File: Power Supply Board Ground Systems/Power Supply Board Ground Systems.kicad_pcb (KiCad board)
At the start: 2 copper layers, 203.2 x 50.8 mm, 38 parts, among them J1 POWER, J2 POWER OUT, SW1 SW_DIP_x01, SW2 SW_DIP_x01, SW3 SW_DIP_x01, SW4 SW_DIP_x01, SW5 SW_DIP_x01, SW6 SW_DIP_x01, SW7 SW_DIP_x01, SW8 SW_DIP_x01

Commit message: Some work
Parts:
- removed D10, D12, D14, D16: D_Small, Diode_SMD:D_SMA
- removed D11, D13, D15, D9: LED, LED_SMD:LED_0805_2012Metric
- removed R5, R6, R7, R8: 2.9K, Resistor_SMD:R_0603_1608Metric
- removed SW5, SW6, SW7, SW8: SW_DIP_x01, Rocker:RockerSwitch
- J2: footprint TerminalBlock_Phoenix:TerminalBlock_Phoenix_MPT-0,5-8-2.54_1x08_P2.54mm_Horizontal -> TerminalBlock_Phoenix:TerminalBlock_Phoenix_MKDS-1,5-4_1x04_P5.00mm_Horizontal
- moved H3 88.9 mm to (135.9, 40.6)
- moved H4 88.9 mm to (135.9, 66.0)
- moved J1 47.9 mm to (79.1, 70.6)
- moved J2 47.3 mm to (89.5, 32.2)
- moved D8 19.7 mm to (107.6, 30.9), turned to 0 degrees
- moved D7 17.4 mm to (105.9, 33.9), turned to 0 degrees
- moved R4 14.9 mm to (109.2, 33.9), turned to 0 degrees
- moved D5 10.4 mm to (95.4, 37.7), turned to 0 degrees
- moved R3 7.49 mm to (98.7, 37.7), turned to 0 degrees
- moved D6 6.96 mm to (97.2, 34.8), turned to 0 degrees
- moved D3 6.50 mm to (68.2, 38.1)
- moved R2 6.50 mm to (64.9, 38.0)
- moved D4 6.50 mm to (66.5, 35.2)
- moved R1 4.69 mm to (53.9, 34.0)
- moved D1 4.69 mm to (57.3, 34.0)
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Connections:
- J2 pad 1: OUT8 -> OUT4
- J2 pad 2: OUT7 -> OUT3
- J2 pad 3: OUT6 -> OUT2
- J2 pad 4: OUT5 -> OUT1
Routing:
- net POW IN: track 0.00 -> 100.8 mm
- net PSW4: track 0.00 -> 31.4 mm
- net PSW1: track 0.00 -> 30.9 mm
- net PSW3: track 0.00 -> 26.8 mm
- net PSW2: track 0.00 -> 26.3 mm
- net OUT1: track 0.00 -> 20.6 mm
- net OUT4: track 0.00 -> 20.0 mm
- net OUT2: track 0.00 -> 15.4 mm
- net OUT3: track 0.00 -> 15.0 mm
- net Net-(D3-Pad2): track 0.00 -> 1.61 mm
- net Net-(D1-Pad2): track 0.00 -> 1.61 mm
- net Net-(D7-Pad2): track 0.00 -> 1.59 mm
- net Net-(D5-Pad2): track 0.00 -> 1.58 mm
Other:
- board size 203.2 x 50.8 mm -> 114.3 x 50.8 mm
- board text added: "AARHUS WUZ HERE"
- board text added: "GND"
- board text added: "IN"
- board text added: "OUT"
- board text added: "POWER DIVIDER"
- board text added: "PWR"

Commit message: PT Board Moment
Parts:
- moved H1 1.27 mm to (30.5, 40.6)
- moved H2 1.27 mm to (30.5, 66.0)
- moved H3 1.27 mm to (134.6, 40.6)
- moved H4 1.27 mm to (134.6, 66.0)
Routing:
- net POW IN: track 100.8 -> 108.9 mm
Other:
- board text added: "CH1"
- board text added: "CH2"
- board text added: "CH3"
- board text added: "CH4"
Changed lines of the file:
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@@
     (property "Sheetname" "")
     (attr smd)
-    (fp_text reference "R4" (at 0 0 90) (layer "F.SilkS")
+    (fp_text reference "R4" (at -0.005 0.02 90) (layer "F.SilkS")
       (effects (font (size 0.5 0.5) (thickness 0.1)))
     )
@@
   )
   (footprint "MountingHole:MountingHole_3.2mm_M3_Pad_TopBottom" (layer "F.Cu")
-    (at 135.89 66.04)
+    (at 134.62 66.04)
     (descr "Mounting Hole 3.2mm, M3")
     (tags "mounting hole 3.2mm m3")
@@
     (property "Sheetname" "")
     (attr through_hole)
-    (fp_text reference "J2" (at 7.5 -6.26) (layer "F.SilkS")
+    (fp_text reference "J2" (at 7.5 -6.26) (layer "F.SilkS") hide
       (effects (font (size 1 1) (thickness 0.15)))
     )
@@
     (property "Sheetname" "")
     (attr through_hole)
-    (fp_text reference "J1" (at 2.45 -6.315) (layer "F.SilkS")
+    (fp_text reference "J1" (at 2.45 -6.315) (layer "F.SilkS") hide
       (effects (font (size 1 1) (thickness 0.15)))
     )
@@
   )
   (footprint "MountingHole:MountingHole_3.2mm_M3_Pad_TopBottom" (layer "F.Cu")
-    (at 29.21 66.04)
+    (at 30.48 66.04)
     (descr "Mounting Hole 3.2mm, M3")
     (tags "mounting hole 3.2mm m3")
@@
   )
   (footprint "MountingHole:MountingHole_3.2mm_M3_Pad_TopBottom" (layer "F.Cu")
-    (at 135.89 40.64)
+    (at 134.62 40.64)
     (descr "Mounting Hole 3.2mm, M3")
     (tags "mounting hole 3.2mm m3")
@@
   )
   (footprint "MountingHole:MountingHole_3.2mm_M3_Pad_TopBottom" (layer "F.Cu")
-    (at 29.21 40.64)
+    (at 30.48 40.64)
     (descr "Mounting Hole 3.2mm, M3")
     (tags "mounting hole 3.2mm m3")
@@
   )
   (gr_rect (start 25.4 25.4) (end 139.7 76.2) (layer "Edge.Cuts") (width 0.1) (fill none))
-  (gr_text "AARHUS WUZ HERE" (at 81.93 39.31) (layer "B.SilkS")
+  (gr_text "AARHUS WUZ HERE" (at 82.71 41.18) (layer "B.SilkS")
     (effects (font (size 1 1) (thickness 0.15)) (justify mirror))
   )
-  (gr_text "POWER DIVIDER" (at 100.01 69.12) (layer "F.SilkS")
-    (effects (font (size 1.5 1.5) (thickness 0.3)))
+  (gr_text "CH4" (at 89.635216 26.4 180) (layer "F.SilkS")
+    (effects (font (size 1 1) (thickness 0.15)))
+  )
+  (gr_text "POWER DIVIDER" (at 108.26 71.78) (layer "F.SilkS")
+    (effects (font (size 2 2) (thickness 0.3)))
+  )
+  (gr_text "POWER DIVIDER" (at 57.77 71.78) (layer "F.SilkS")
+    (effects (font (size 2 2) (thickness 0.3)))
   )
   (gr_text "PWR" (at 88.81 75.06) (layer "F.SilkS")
@@
     (effects (font (size 1 1) (thickness 0.15)))
   )
+  (gr_text "CH1" (at 74.357392 26.4 180) (layer "F.SilkS")
+    (effects (font (size 1 1) (thickness 0.15)))
+  )
   (gr_text "OUT" (at 128.53 28.92 180) (layer "F.SilkS")
     (effects (font (size 3 3) (thickness 0.3)))
@@
     (effects (font (size 3 3) (thickness 0.3)))
   )
+  (gr_text "CH2" (at 79.45 26.4 180) (layer "F.SilkS")
+    (effects (font (size 1 1) (thickness 0.15)))
+  )
   (gr_text "IN" (at 37.03 72.82) (layer "F.SilkS")
     (effects (font (size 3 3) (thickness 0.3)))
+  )
+  (gr_text "CH3" (at 84.542608 26.4 180) (layer "F.SilkS")
+    (effects (font (size 1 1) (thickness 0.15)))
   )
   (gr_text "OUT" (at 37.18 28.92 180) (layer "F.SilkS")
@@
   (segment (start 119.58 36.92) (end 113.54 30.88) (width 1) (layer "F.Cu") (net 12))
   (segment (start 110.06 32.85) (end 109.64 32.43) (width 0.3) (layer "F.Cu") (net 12))
-  (segment (start 80.58 65.71) (end 84.1 69.23) (width 3) (layer "F.Cu") (net 13))
-  (segment (start 119.58 59.73) (end 113.67 65.64) (width 3) (layer "F.Cu") (net 13))
-  (segment (start 47.03 65.71) (end 72.74 65.71) (width 3) (layer "F.Cu") (net 13))
-  (segment (start 89.085 65.64) (end 84.1 70.625) (width 3) (layer "F.Cu") (net 13))
-  (segment (start 45.15 59.73) (end 45.15 63.83) (width 3) (layer "F.Cu") (net 13))
-  (segment (start 84.1 69.23) (end 84.1 70.625) (width 3) (layer "F.Cu") (net 13))
-  (segment (start 69.96 59.73) (end 69.96 62.93) (width 3) (layer "F.Cu") (net 13))
-  (segment (start 94.77 59.73) (end 94.77 63.09) (width 3) (layer "F.Cu") (net 13))
-  (segment (start 69.96 62.93) (end 72.74 65.71) (width 3) (layer "F.Cu") (net 13))
-  (segment (start 72.74 65.71) (end 80.58 65.71) (width 3) (layer "F.Cu") (net 13))
-  (segment (start 94.77 63.09) (end 97.32 65.64) (width 3) (layer "F.Cu") (net 13))
-  (segment (start 113.67 65.64) (end 97.32 65.64) (width 3) (layer "F.Cu") (net 13))
-  (segment (start 97.32 65.64) (end 89.085 65.64) (width 3) (layer "F.Cu") (net 13))
-  (segment (start 45.15 63.83) (end 47.03 65.71) (width 3) (layer "F.Cu") (net 13))
+  (segment (start 119.58 62.98) (end 115.91 66.65) (width 1) (layer "F.Cu") (net 13))
+  (segment (start 84.1 70.625) (end 84.1 68.786523) (width 3) (layer "F.Cu") (net 13))
+  (segment (start 45.15 64.03) (end 47.71 66.59) (width 1) (layer "F.Cu") (net 13))
+  (segment (start 45.15 59.73) (end 45.15 64.03) (width 1) (layer "F.Cu") (net 13))
+  (segment (start 90.92 66.66) (end 90.31 66.66) (width 1) (layer "F.Cu") (net 13))
+  (segment (start 88.065 66.66) (end 90.31 66.66) (width 3) (layer "F.Cu") (net 13))
+  (segment (start 81.903477 66.59) (end 73.66 66.59) (width 3) (layer "F.Cu") (net 13))
+  (segment (start 119.58 59.73) (end 119.58 62.98) (width 1) (layer "F.Cu") (net 13))
+  (segment (start 94.77 59.73) (end 94.77 62.81) (width 1) (layer "F.Cu") (net 13))
+  (segment (start 73.66 66.59) (end 47.71 66.59) (width 3) (layer "F.Cu") (net 13))
+  (segment (start 90.31 66.66) (end 90.41 66.56) (width 3) (layer "F.Cu") (net 13))
+  (segment (start 88.065 66.66) (end 115.9 66.66) (width 3) (layer "F.Cu") (net 13))
+  (segment (start 94.77 62.81) (end 90.92 66.66) (width 1) (layer "F.Cu") (net 13))
+  (segment (start 84.1 68.786523) (end 81.903477 66.59) (width 3) (layer "F.Cu") (net 13))
+  (segment (start 115.9 66.66) (end 115.91 66.65) (width 3) (layer "F.Cu") (net 13))
+  (segment (start 69.96 59.73) (end 69.96 62.89) (width 1) (layer "F.Cu") (net 13))
+  (segment (start 69.96 62.89) (end 73.66 66.59) (width 1) (layer "F.Cu") (net 13))
+  (segment (start 84.1 70.625) (end 88.065 66.66) (width 3) (layer "F.Cu") (net 13))
   (zone (net 14) (net_name "GND") (layer "B.Cu") (hatch edge 0.508)
     (connect_pads yes (clearance 0.508))

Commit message: Idk lol some format changes
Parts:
- moved D8 36.9 mm to (121.3, 65.2), turned to -90 degrees
- moved D2 36.1 mm to (44.1, 65.3), turned to -90 degrees
- moved R4 34.1 mm to (118.3, 66.8), turned to -90 degrees
- moved R1 33.6 mm to (47.0, 66.9), turned to -90 degrees
- moved D7 32.0 mm to (118.3, 63.4), turned to -90 degrees
- moved D1 31.3 mm to (47.0, 63.5), turned to -90 degrees
- moved D6 30.3 mm to (96.1, 65.1), turned to -90 degrees
- moved D4 30.1 mm to (69.2, 65.1), turned to -90 degrees
- moved R2 29.6 mm to (72.1, 66.8), turned to -90 degrees
- moved R3 29.5 mm to (93.3, 66.7), turned to -90 degrees
- moved D5 25.7 mm to (93.2, 63.3), turned to -90 degrees
- moved D3 25.6 mm to (72.1, 63.4), turned to -90 degrees
- moved SW4 4.23 mm to (121.2, 48.8)
- moved SW3 4.14 mm to (96.2, 48.8)
- moved SW1 4.06 mm to (44.0, 48.8)
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- renumbered H3 to Hw
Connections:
- D1 pad 1: OUT1 -> PSW1
- D2 pad 1: OUT1 -> PSW1
- D2 pad 2: PSW1 -> POW IN
- D3 pad 1: OUT2 -> PSW2
- D4 pad 1: OUT2 -> PSW2
- D4 pad 2: PSW2 -> POW IN
- D5 pad 1: OUT3 -> PSW3
- D6 pad 1: OUT3 -> PSW3
- D6 pad 2: PSW3 -> POW IN
- D7 pad 1: OUT4 -> PSW4
- D8 pad 1: OUT4 -> PSW4
- D8 pad 2: PSW4 -> POW IN
- R1 pad 2: PSW1 -> POW IN
- R2 pad 2: PSW2 -> POW IN
- R3 pad 2: PSW3 -> POW IN
- R4 pad 2: PSW4 -> POW IN
- SW1 pad 1: POW IN -> PSW1
- SW1 pad 2: PSW1 -> OUT1
- SW2 pad 1: POW IN -> PSW2
- SW2 pad 2: PSW2 -> OUT2
- SW3 pad 1: POW IN -> PSW3
- SW3 pad 2: PSW3 -> OUT3
- SW4 pad 1: POW IN -> PSW4
- SW4 pad 2: PSW4 -> OUT4
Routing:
- net PSW4: track 31.4 -> 10.9 mm
- net PSW1: track 30.9 -> 10.8 mm
- net OUT4: track 20.0 -> 38.4 mm
- net OUT1: track 20.6 -> 38.1 mm
- net PSW3: track 26.8 -> 10.5 mm
- net PSW2: track 26.3 -> 10.5 mm
- net OUT3: track 15.0 -> 26.0 mm
- net POW IN: track 108.9 -> 119.5 mm
- net OUT2: track 15.4 -> 25.4 mm

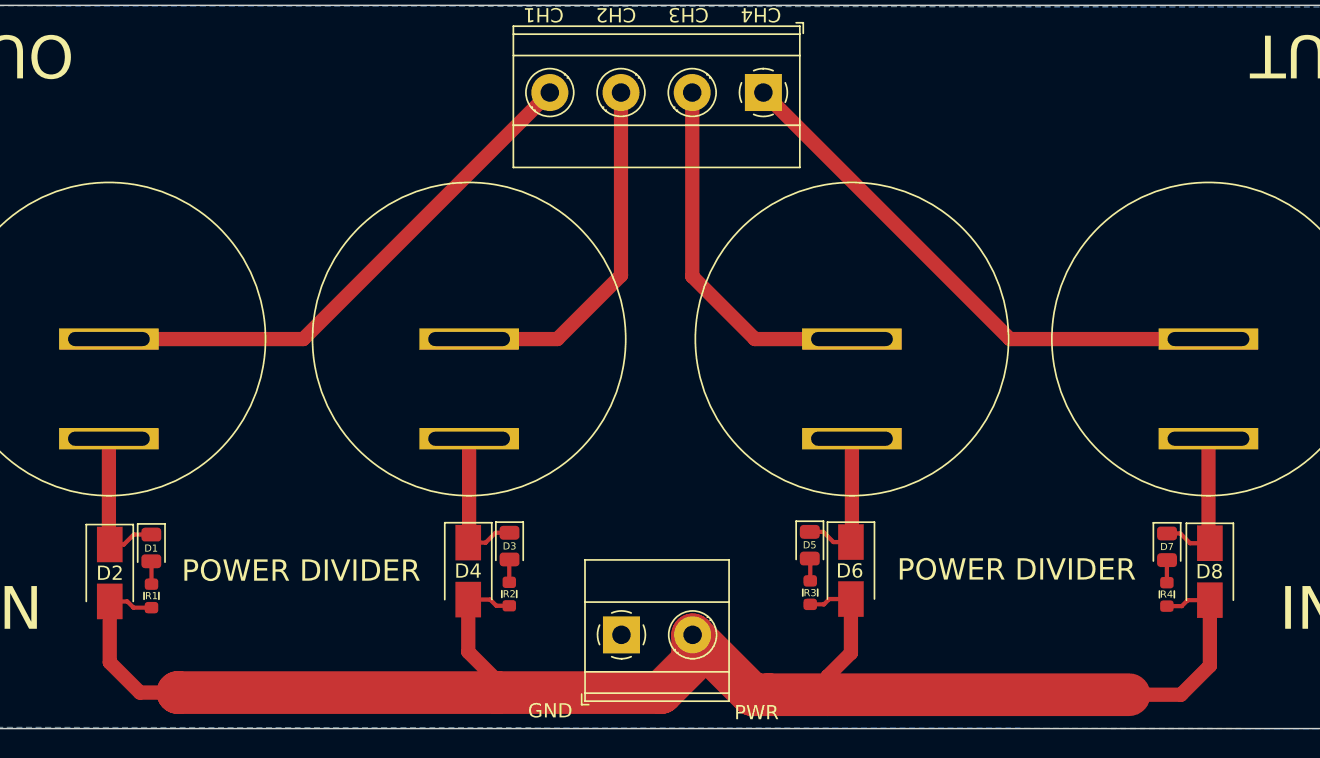
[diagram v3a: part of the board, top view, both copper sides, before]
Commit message: Reconfigured the LEDs
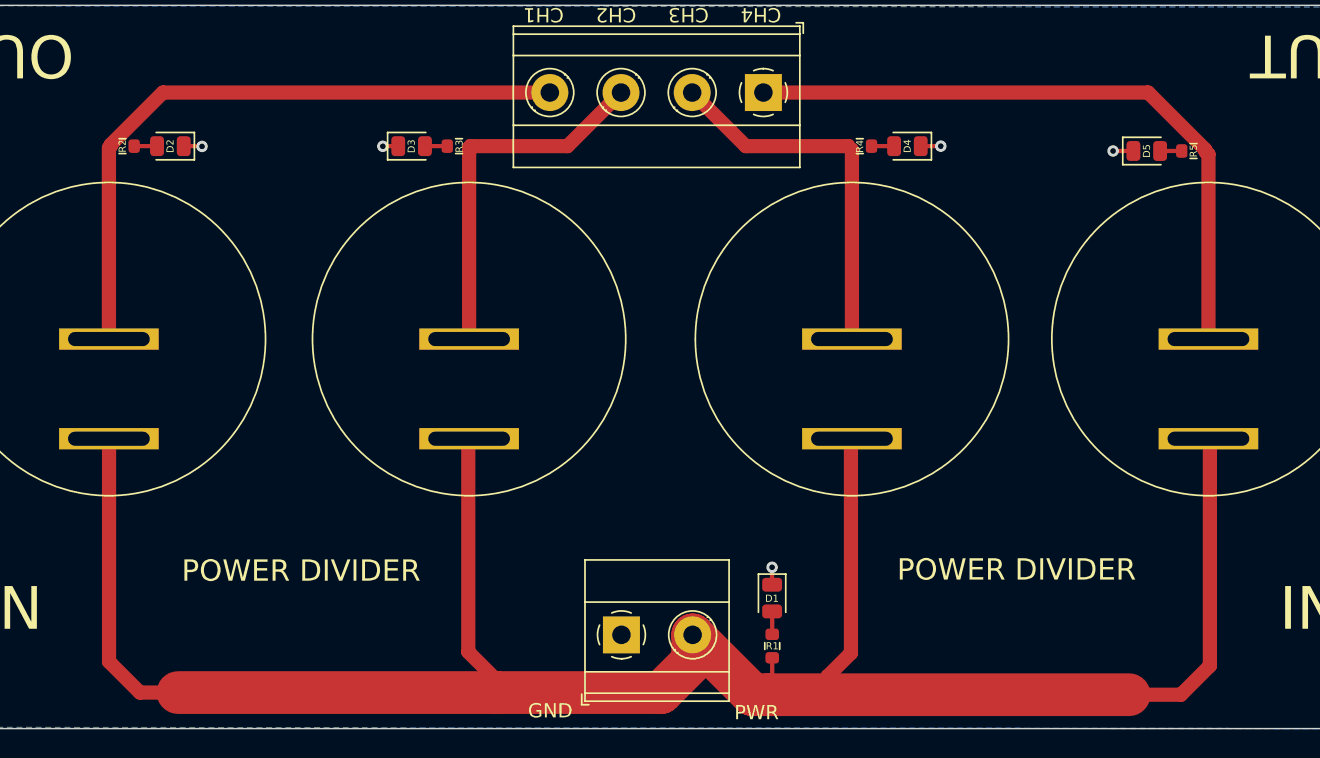
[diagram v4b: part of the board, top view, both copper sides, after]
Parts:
- removed the D2 at (44.1, 65.3)
- removed the D4 at (69.2, 65.1)
- removed D6, D8: D_Small, Diode_SMD:D_SMA
- added D5: LED, LED_SMD:LED_0805_2012Metric, F.Cu at (116.9, 35.6)
- added R5: 8K, Resistor_SMD:R_0603_1608Metric, F.Cu at (120.2, 35.6)
- R1, R2, R3, R4: value 2.9K -> 8K
- moved D1 43.7 mm to (90.6, 67.0)
- moved R1 43.7 mm to (90.6, 70.4)
- moved R2 41.6 mm to (45.0, 35.3), turned to 180 degrees
- moved R3 39.9 mm to (68.6, 35.3), turned to 0 degrees
- moved D3 39.6 mm to (65.3, 35.3), turned to 0 degrees
- moved R4 38.2 mm to (96.7, 35.3), turned to 180 degrees
- moved D2 36.8 mm to (48.3, 35.3), turned to 180 degrees
- moved D4 33.5 mm to (100.1, 35.3), turned to 180 degrees
- renumbered D3 to D2, D5 to D3, D7 to D4, Hw to H3
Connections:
- D1 pad 1: PSW1 -> GND
- D2 pad 1: PSW2 -> GND
- D3 pad 1: PSW3 -> GND
- D4 pad 1: PSW4 -> GND
- R2 pad 2: POW IN -> OUT1
- R3 pad 2: POW IN -> OUT2
- R4 pad 2: POW IN -> OUT3
- SW1 pad 1: PSW1 -> POW IN
- SW2 pad 1: PSW2 -> POW IN
- SW3 pad 1: PSW3 -> POW IN
- SW4 pad 1: PSW4 -> POW IN
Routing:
- net POW IN: track 119.5 -> 155.3 mm
- net PSW4: track 10.9 -> 0.00 mm
- net PSW1: track 10.8 -> 0.00 mm
- net PSW2: track 10.5 -> 0.00 mm
- net PSW3: track 10.5 -> 0.00 mm
- net OUT1: track 38.1 -> 46.1 mm
- net OUT4: track 38.4 -> 46.1 mm
- net GND: track 0.00 -> 6.44 mm, vias 0 -> 5
- net Net-(D5-Pad2): track 0.00 -> 1.53 mm

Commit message: Added stitches
Needs footprints made
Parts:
- removed SW1, SW2, SW3, SW4: SW_DIP_x01, Rocker:RockerSwitch
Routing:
- net POW IN: track 155.3 -> 0.00 mm
- net OUT4: track 46.1 -> 0.00 mm
- net OUT1: track 46.1 -> 0.00 mm
- net OUT3: track 26.2 -> 0.00 mm
- net OUT2: track 25.7 -> 0.00 mm
- net GND: track 6.44 -> 0.00 mm
- net Net-(D2-Pad2): track 1.61 -> 0.00 mm
- net Net-(D1-Pad2): track 1.61 -> 0.00 mm
- net Net-(D4-Pad2): track 1.58 -> 0.00 mm
- net Net-(D3-Pad2): track 1.57 -> 0.00 mm
- net Net-(D5-Pad2): track 1.53 -> 0.00 mm

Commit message: Re Done Power Supply Board
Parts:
- added D6: LED, LED_SMD:LED_0805_2012Metric, F.Cu at (66.5, 39.8)
- added D7: LED, LED_SMD:LED_0805_2012Metric, F.Cu at (74.2, 39.8)
- added D8: LED, LED_SMD:LED_0805_2012Metric, F.Cu at (81.9, 39.8)
- added D9: LED, LED_SMD:LED_0805_2012Metric, F.Cu at (89.6, 39.8)
- added R6: 8K, Resistor_SMD:R_0603_1608Metric, F.Cu at (69.0, 42.3)
- added R7: 8K, Resistor_SMD:R_0603_1608Metric, F.Cu at (76.7, 42.3)
- added R8: 8K, Resistor_SMD:R_0603_1608Metric, F.Cu at (84.4, 42.3)
- added R9: 8K, Resistor_SMD:R_0603_1608Metric, F.Cu at (92.1, 42.3)
- added SW1: SW_SPDT, E_Switch:100SP1T1B1M2QEH, F.Cu at (35.7, 46.5)
- added SW2: SW_SPDT, E_Switch:100SP1T1B1M2QEH, F.Cu at (43.4, 46.5)
- added SW3: SW_SPDT, E_Switch:100SP1T1B1M2QEH, F.Cu at (51.1, 46.5)
- added SW4: SW_SPDT, E_Switch:100SP1T1B1M2QEH, F.Cu at (58.8, 46.5)
- added SW5: SW_SPDT, E_Switch:100SP1T1B1M2QEH, F.Cu at (66.5, 46.5)
- added SW6: SW_SPDT, E_Switch:100SP1T1B1M2QEH, F.Cu at (74.2, 46.5)
- added SW7: SW_SPDT, E_Switch:100SP1T1B1M2QEH, F.Cu at (81.9, 46.5)
- added SW8: SW_SPDT, E_Switch:100SP1T1B1M2QEH, F.Cu at (89.5, 46.5)
- J2: footprint TerminalBlock_Phoenix:TerminalBlock_Phoenix_MKDS-1,5-4_1x04_P5.00mm_Horizontal -> TerminalBlock_Phoenix:TerminalBlock_Phoenix_MKDS-1,5-8_1x08_P5.00mm_Horizontal
- moved R5 59.3 mm to (61.3, 42.3)
- moved D5 58.2 mm to (58.8, 39.8), turned to -90 degrees
- moved D4 49.2 mm to (51.1, 39.8), turned to -90 degrees
- moved R4 43.7 mm to (53.6, 42.3), turned to 0 degrees
- moved H3 38.1 mm to (96.5, 38.1)
- moved H4 38.1 mm to (96.5, 63.5)
- moved R3 23.7 mm to (45.9, 42.3)
- moved D3 22.3 mm to (43.4, 39.8), turned to -90 degrees
- moved J1 20.0 mm to (60.0, 69.1)
- moved R1 19.0 mm to (71.6, 69.1), turned to 180 degrees
- moved D1 15.7 mm to (75.0, 69.1), turned to 180 degrees
- moved D2 13.4 mm to (35.7, 39.8), turned to -90 degrees
- moved J2 11.9 mm to (78.0, 31.8)
- moved R2 9.72 mm to (38.2, 42.3), turned to 0 degrees
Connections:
- J2 pad 1: OUT4 -> OUT8
- J2 pad 2: OUT3 -> OUT7
- J2 pad 3: OUT2 -> OUT6
- J2 pad 4: OUT1 -> OUT5
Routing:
- net POW IN: track 0.00 -> 123.4 mm
- net OUT8: track 0.00 -> 32.0 mm
- net OUT7: track 0.00 -> 30.4 mm
- net OUT6: track 0.00 -> 27.0 mm
- net OUT5: track 0.00 -> 24.2 mm
- net OUT4: track 0.00 -> 23.8 mm
- net OUT1: track 0.00 -> 23.3 mm
- net OUT2: track 0.00 -> 22.9 mm
- net OUT3: track 0.00 -> 22.5 mm
- net GND: track 0.00 -> 11.9 mm, vias 5 -> 9
- net Net-(D2-Pad2): track 0.00 -> 3.00 mm
- net Net-(D5-Pad2): track 0.00 -> 2.96 mm
- net Net-(D8-Pad2): track 0.00 -> 2.94 mm
- net Net-(D9-Pad2): track 0.00 -> 2.94 mm
- net Net-(D4-Pad2): track 0.00 -> 2.89 mm
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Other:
- board size 114.3 x 50.8 mm -> 76.2 x 50.8 mm
- board text added: "CH5"
- board text added: "CH6"
- board text added: "CH7"
- board text added: "CH8"

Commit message: AGS Board Work
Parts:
- moved R1 1.31 mm to (70.3, 69.1)
- moved D1 1.31 mm to (73.7, 69.1)
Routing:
- net POW IN: track 123.4 -> 122.2 mm
- net GND: track 11.9 -> 11.1 mm

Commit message: Power Line Changes
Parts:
- J1: footprint TerminalBlock_Phoenix:TerminalBlock_Phoenix_MKDS-1,5-2_1x02_P5.00mm_Horizontal -> TerminalBlock_Phoenix:TerminalBlock_Phoenix_MPT-0,5-2-2.54_1x02_P2.54mm_Horizontal
- J2: footprint TerminalBlock_Phoenix:TerminalBlock_Phoenix_MKDS-1,5-8_1x08_P5.00mm_Horizontal -> TerminalBlock_Phoenix:TerminalBlock_Phoenix_MPT-0,5-8-2.54_1x08_P2.54mm_Horizontal
- moved D1 19.3 mm to (56.9, 59.6), turned to 0 degrees
- moved R1 13.9 mm to (60.2, 59.6), turned to 0 degrees
- moved J1 10.3 mm to (63.8, 59.5)
- moved H1 6.35 mm to (30.5, 31.8)
- moved H2 6.35 mm to (30.5, 57.1)
- moved H3 6.35 mm to (96.5, 31.8)
- moved H4 6.35 mm to (96.5, 57.1)
- moved D6 3.19 mm to (67.6, 36.8)
- moved D7 3.19 mm to (75.3, 36.8)
- moved D8 3.19 mm to (83.0, 36.8)
- moved R3 3.19 mm to (47.0, 39.3)
- moved R5 3.19 mm to (62.4, 39.3)
- moved R7 3.19 mm to (77.8, 39.3)
- moved R8 3.19 mm to (85.5, 39.3)
- moved SW3 3.19 mm to (52.2, 43.5)
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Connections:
- J1 pad 1: GND -> POW IN
- J1 pad 2: POW IN -> GND
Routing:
- net POW IN: track 122.2 -> 0.00 mm
- net OUT1: track 23.7 -> 36.1 mm
- net OUT2: track 22.9 -> 30.9 mm
- net OUT3: track 22.5 -> 25.4 mm
- net OUT5: track 24.2 -> 21.3 mm
- net OUT8: track 32.0 -> 34.8 mm
- net OUT4: track 23.8 -> 21.5 mm
- net OUT7: track 30.4 -> 32.1 mm
- net OUT6: track 27.0 -> 25.8 mm
- added copper zone on F.Cu, net POW IN
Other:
- board size 76.2 x 50.8 mm -> 76.2 x 38.1 mm
